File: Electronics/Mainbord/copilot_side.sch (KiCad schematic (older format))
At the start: 30 parts, among them U50 74HC165, U51 74HC165, U52 74HC165, U53 74HC165, U54 4067, U55 74HC4051

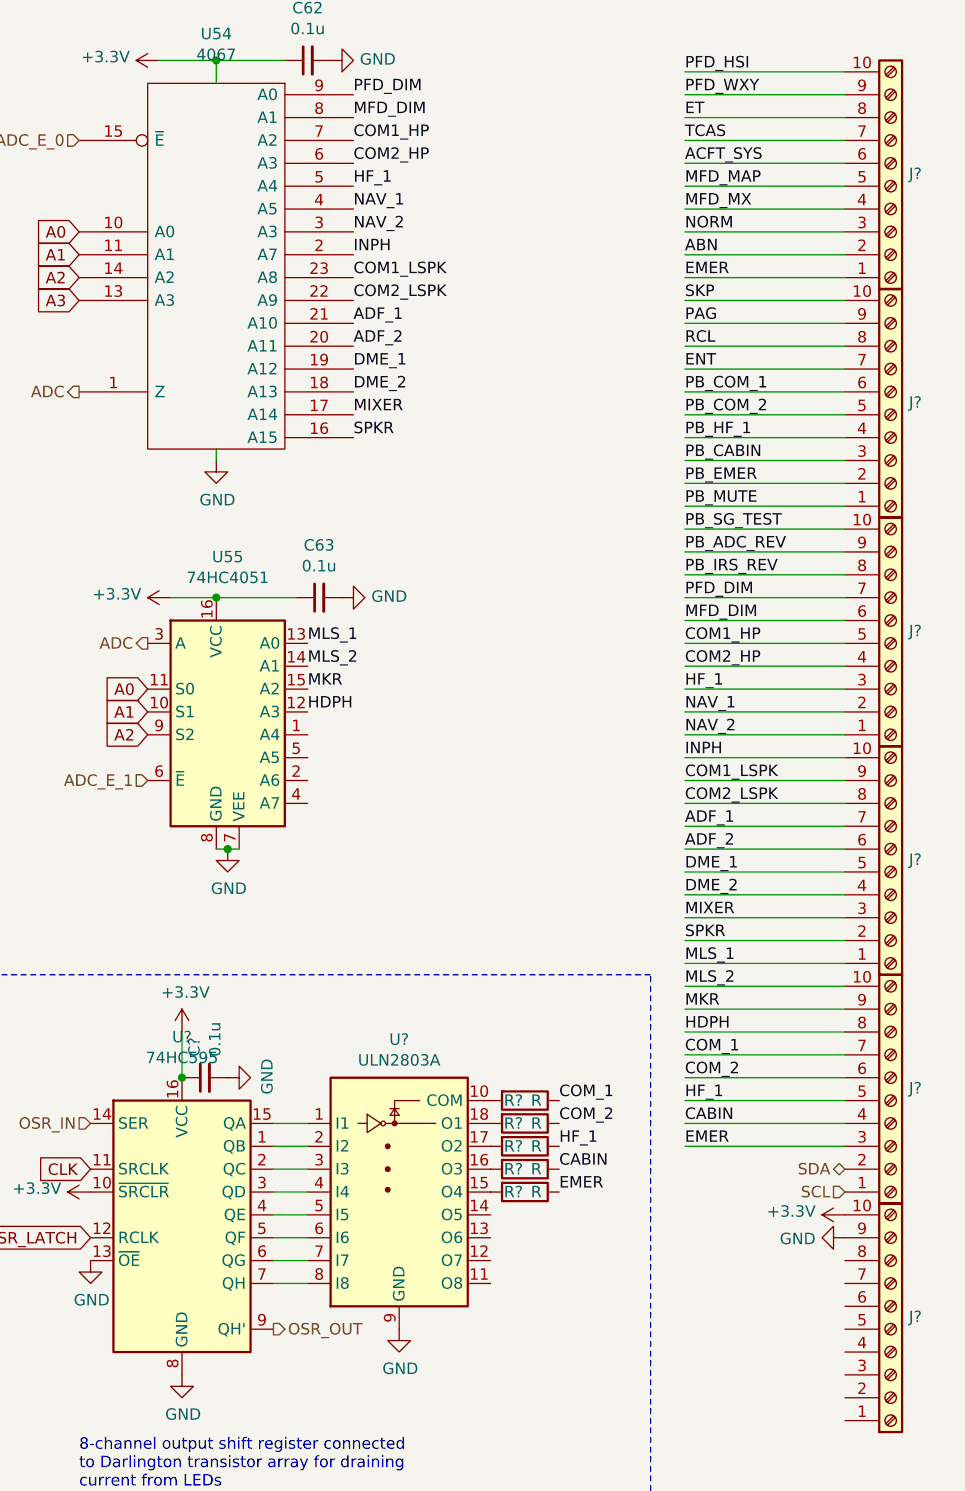
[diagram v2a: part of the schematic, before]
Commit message: Electronics - Adds LCSC part numbers and footprints
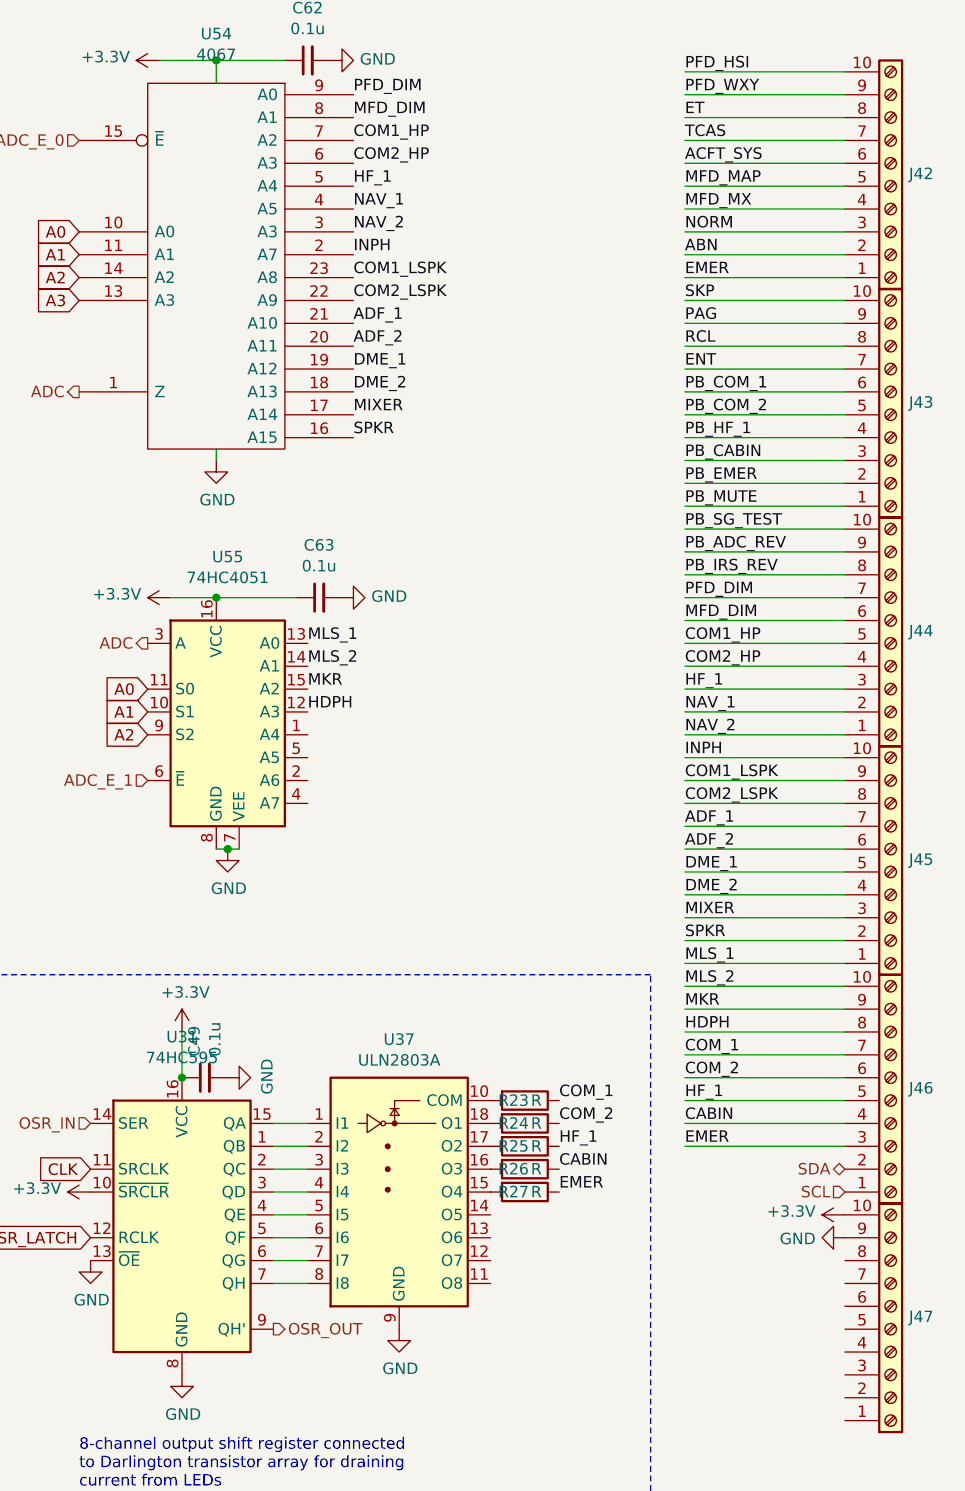
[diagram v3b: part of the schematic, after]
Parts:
- gave numbers to parts that had none: 14
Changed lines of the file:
@@
 AR Path="/5DB6029E/5DF7CBB3" Ref="J?"  Part="1"
 AR Path="/5DC174D4/5DF7CBB3" Ref="J?"  Part="1"
-AR Path="/5DC31399/5DF7CBB3" Ref="J?"  Part="1"
-F 0 "J?" H 8680 1546 50  0000 L CNN
+AR Path="/5DC31399/5DF7CBB3" Ref="J42"  Part="1"
+F 0 "J42" H 8680 1546 50  0000 L CNN
 F 1 "Screw_Terminal_01x10" H 8520 966 50  0001 C CNN
 F 2 "" H 8600 1600 50  0001 C CNN
@@
 AR Path="/5DB6029E/5DF7CBCA" Ref="J?"  Part="1"
 AR Path="/5DC174D4/5DF7CBCA" Ref="J?"  Part="1"
-AR Path="/5DC31399/5DF7CBCA" Ref="J?"  Part="1"
-F 0 "J?" H 8680 2546 50  0000 L CNN
+AR Path="/5DC31399/5DF7CBCA" Ref="J43"  Part="1"
+F 0 "J43" H 8680 2546 50  0000 L CNN
 F 1 "Screw_Terminal_01x10" H 8520 1966 50  0001 C CNN
 F 2 "" H 8600 2600 50  0001 C CNN
@@
 AR Path="/5DB6029E/5DF7CBF0" Ref="J?"  Part="1"
 AR Path="/5DC174D4/5DF7CBF0" Ref="J?"  Part="1"
-AR Path="/5DC31399/5DF7CBF0" Ref="J?"  Part="1"
-F 0 "J?" H 8680 3546 50  0000 L CNN
+AR Path="/5DC31399/5DF7CBF0" Ref="J44"  Part="1"
+F 0 "J44" H 8680 3546 50  0000 L CNN
 F 1 "Screw_Terminal_01x10" H 8520 2966 50  0001 C CNN
 F 2 "" H 8600 3600 50  0001 C CNN
@@
 AR Path="/5DB6029E/5DF7CBFD" Ref="J?"  Part="1"
 AR Path="/5DC174D4/5DF7CBFD" Ref="J?"  Part="1"
-AR Path="/5DC31399/5DF7CBFD" Ref="J?"  Part="1"
-F 0 "J?" H 8680 4546 50  0000 L CNN
+AR Path="/5DC31399/5DF7CBFD" Ref="J45"  Part="1"
+F 0 "J45" H 8680 4546 50  0000 L CNN
 F 1 "Screw_Terminal_01x10" H 8520 3966 50  0001 C CNN
 F 2 "" H 8600 4600 50  0001 C CNN
@@
 AR Path="/5DB6029E/5DF7CC14" Ref="J?"  Part="1"
 AR Path="/5DC174D4/5DF7CC14" Ref="J?"  Part="1"
-AR Path="/5DC31399/5DF7CC14" Ref="J?"  Part="1"
-F 0 "J?" H 8680 5546 50  0000 L CNN
+AR Path="/5DC31399/5DF7CC14" Ref="J46"  Part="1"
+F 0 "J46" H 8680 5546 50  0000 L CNN
 F 1 "Screw_Terminal_01x10" H 8520 4966 50  0001 C CNN
 F 2 "" H 8600 5600 50  0001 C CNN
@@
 AR Path="/5DB6029E/5DF95124" Ref="J?"  Part="1"
 AR Path="/5DC174D4/5DF95124" Ref="J?"  Part="1"
-AR Path="/5DC31399/5DF95124" Ref="J?"  Part="1"
-F 0 "J?" H 8680 6546 50  0000 L CNN
+AR Path="/5DC31399/5DF95124" Ref="J47"  Part="1"
+F 0 "J47" H 8680 6546 50  0000 L CNN
 F 1 "Screw_Terminal_01x10" H 8520 5966 50  0001 C CNN
 F 2 "" H 8600 6600 50  0001 C CNN
@@
 AR Path="/5DB5DCD1/5DFA1204" Ref="#PWR?"  Part="1"
 AR Path="/5DC174D4/5DFA1204" Ref="#PWR?"  Part="1"
-AR Path="/5DC31399/5DFA1204" Ref="#PWR?"  Part="1"
-F 0 "#PWR?" H 8400 5950 50  0001 C CNN
+AR Path="/5DC31399/5DFA1204" Ref="#PWR0279"  Part="1"
+F 0 "#PWR0279" H 8400 5950 50  0001 C CNN
 F 1 "+3.3V" V 8415 6228 50  0000 L CNN
 F 2 "" H 8400 6100 50  0001 C CNN
@@
 AR Path="/5DB5DCD1/5DFA1241" Ref="#PWR?"  Part="1"
 AR Path="/5DC174D4/5DFA1241" Ref="#PWR?"  Part="1"
-AR Path="/5DC31399/5DFA1241" Ref="#PWR?"  Part="1"
-F 0 "#PWR?" H 8400 5950 50  0001 C CNN
+AR Path="/5DC31399/5DFA1241" Ref="#PWR0280"  Part="1"
+F 0 "#PWR0280" H 8400 5950 50  0001 C CNN
 F 1 "GND" V 8405 6072 50  0000 R CNN
 F 2 "" H 8400 6200 50  0001 C CNN
@@
 AR Path="/5DB5DCD1/5E013912" Ref="C?"  Part="1"
 AR Path="/5DC174D4/5E013912" Ref="C?"  Part="1"
-AR Path="/5DC31399/5E013912" Ref="C?"  Part="1"
-F 0 "C?" H 5692 5546 50  0000 L CNN
+AR Path="/5DC31399/5E013912" Ref="C49"  Part="1"
+F 0 "C49" H 5692 5546 50  0000 L CNN
 F 1 "0.1u" H 5692 5455 50  0000 L CNN
 F 2 "" H 5600 5500 50  0001 C CNN
@@
 AR Path="/5DB5DCD1/5E013919" Ref="#PWR?"  Part="1"
 AR Path="/5DC174D4/5E013919" Ref="#PWR?"  Part="1"
-AR Path="/5DC31399/5E013919" Ref="#PWR?"  Part="1"
-F 0 "#PWR?" H 5700 5250 50  0001 C CNN
+AR Path="/5DC31399/5E013919" Ref="#PWR0281"  Part="1"
+F 0 "#PWR0281" H 5700 5250 50  0001 C CNN
 F 1 "GND" H 5705 5327 50  0000 C CNN
 F 2 "" H 5700 5500 50  0001 C CNN
@@
 AR Path="/5DB5DCD1/5E013920" Ref="U?"  Part="1"
 AR Path="/5DC174D4/5E013920" Ref="U?"  Part="1"
-AR Path="/5DC31399/5E013920" Ref="U?"  Part="1"
-F 0 "U?" H 5500 6878 50  0000 C CNN
+AR Path="/5DC31399/5E013920" Ref="U31"  Part="1"
+F 0 "U31" H 5500 6878 50  0000 C CNN
 F 1 "74HC595" H 5500 6787 50  0000 C CNN
 F 2 "" H 5500 6100 50  0001 C CNN
@@
 AR Path="/5DB5DCD1/5E013928" Ref="#PWR?"  Part="1"
 AR Path="/5DC174D4/5E013928" Ref="#PWR?"  Part="1"
-AR Path="/5DC31399/5E013928" Ref="#PWR?"  Part="1"
-F 0 "#PWR?" H 5500 6550 50  0001 C CNN
+AR Path="/5DC31399/5E013928" Ref="#PWR0282"  Part="1"
+F 0 "#PWR0282" H 5500 6550 50  0001 C CNN
 F 1 "GND" H 5505 6627 50  0000 C CNN
 F 2 "" H 5500 6800 50  0001 C CNN
@@
 AR Path="/5DB5DCD1/5E01392F" Ref="#PWR?"  Part="1"
 AR Path="/5DC174D4/5E01392F" Ref="#PWR?"  Part="1"
-AR Path="/5DC31399/5E01392F" Ref="#PWR?"  Part="1"
-F 0 "#PWR?" H 5100 6050 50  0001 C CNN
+AR Path="/5DC31399/5E01392F" Ref="#PWR0283"  Part="1"
+F 0 "#PWR0283" H 5100 6050 50  0001 C CNN
 F 1 "GND" H 5105 6127 50  0000 C CNN
 F 2 "" H 5100 6300 50  0001 C CNN
@@
 AR Path="/5DB5DCD1/5E013936" Ref="#PWR?"  Part="1"
 AR Path="/5DC174D4/5E013936" Ref="#PWR?"  Part="1"
-AR Path="/5DC31399/5E013936" Ref="#PWR?"  Part="1"
-F 0 "#PWR?" H 5500 5150 50  0001 C CNN
+AR Path="/5DC31399/5E013936" Ref="#PWR0284"  Part="1"
+F 0 "#PWR0284" H 5500 5150 50  0001 C CNN
 F 1 "+3.3V" H 5515 5473 50  0000 C CNN
 F 2 "" H 5500 5300 50  0001 C CNN
@@
 AR Path="/5DB5DCD1/5E01393C" Ref="#PWR?"  Part="1"
 AR Path="/5DC174D4/5E01393C" Ref="#PWR?"  Part="1"
-AR Path="/5DC31399/5E01393C" Ref="#PWR?"  Part="1"
-F 0 "#PWR?" H 5100 5850 50  0001 C CNN
+AR Path="/5DC31399/5E01393C" Ref="#PWR0306"  Part="1"
+F 0 "#PWR0306" H 5100 5850 50  0001 C CNN
 F 1 "+3.3V" V 5115 6128 50  0000 L CNN
 F 2 "" H 5100 6000 50  0001 C CNN
@@
 AR Path="/5DBF6FEB/5E01394A" Ref="U?"  Part="1"
 AR Path="/5DC33C09/5E01394A" Ref="U?"  Part="1"
-AR Path="/5DC31399/5E01394A" Ref="U?"  Part="1"
+AR Path="/5DC31399/5E01394A" Ref="U37"  Part="1"
 AR Path="/5DC174D4/5E01394A" Ref="U?"  Part="1"
-F 0 "U?" H 6450 6467 50  0000 C CNN
+F 0 "U37" H 6450 6467 50  0000 C CNN
 F 1 "ULN2803A" H 6450 6376 50  0000 C CNN
 F 2 "" H 6500 5250 50  0001 L CNN
@@
 AR Path="/5DB5DCD1/5E013951" Ref="#PWR?"  Part="1"
 AR Path="/5DC174D4/5E013951" Ref="#PWR?"  Part="1"
-AR Path="/5DC31399/5E013951" Ref="#PWR?"  Part="1"
-F 0 "#PWR?" H 6450 6350 50  0001 C CNN
+AR Path="/5DC31399/5E013951" Ref="#PWR0307"  Part="1"
+F 0 "#PWR0307" H 6450 6350 50  0001 C CNN
 F 1 "GND" H 6455 6427 50  0000 C CNN
 F 2 "" H 6450 6600 50  0001 C CNN
@@
 P 7000 5600
 AR Path="/5DC33C09/5E013957" Ref="R?"  Part="1"
-AR Path="/5DC31399/5E013957" Ref="R?"  Part="1"
+AR Path="/5DC31399/5E013957" Ref="R23"  Part="1"
 AR Path="/5DC174D4/5E013957" Ref="R?"  Part="1"
-F 0 "R?" V 7000 5550 50  0000 C CNN
+F 0 "R23" V 7000 5550 50  0000 C CNN
 F 1 "R" V 7000 5650 50  0000 C CNN
 F 2 "" V 6930 5600 50  0001 C CNN
@@
 P 7000 5700
 AR Path="/5DC33C09/5E01395E" Ref="R?"  Part="1"
-AR Path="/5DC31399/5E01395E" Ref="R?"  Part="1"
+AR Path="/5DC31399/5E01395E" Ref="R24"  Part="1"
 AR Path="/5DC174D4/5E01395E" Ref="R?"  Part="1"
-F 0 "R?" V 7000 5650 50  0000 C CNN
+F 0 "R24" V 7000 5650 50  0000 C CNN
 F 1 "R" V 7000 5750 50  0000 C CNN
 F 2 "" V 6930 5700 50  0001 C CNN
@@
 P 7000 5800
 AR Path="/5DC33C09/5E013965" Ref="R?"  Part="1"
-AR Path="/5DC31399/5E013965" Ref="R?"  Part="1"
+AR Path="/5DC31399/5E013965" Ref="R25"  Part="1"
 AR Path="/5DC174D4/5E013965" Ref="R?"  Part="1"
-F 0 "R?" V 7000 5750 50  0000 C CNN
+F 0 "R25" V 7000 5750 50  0000 C CNN
 F 1 "R" V 7000 5850 50  0000 C CNN
 F 2 "" V 6930 5800 50  0001 C CNN
@@
 P 7000 5900
 AR Path="/5DC33C09/5E01396C" Ref="R?"  Part="1"
-AR Path="/5DC31399/5E01396C" Ref="R?"  Part="1"
+AR Path="/5DC31399/5E01396C" Ref="R26"  Part="1"
 AR Path="/5DC174D4/5E01396C" Ref="R?"  Part="1"
-F 0 "R?" V 7000 5850 50  0000 C CNN
+F 0 "R26" V 7000 5850 50  0000 C CNN
 F 1 "R" V 7000 5950 50  0000 C CNN
 F 2 "" V 6930 5900 50  0001 C CNN
@@
 P 7000 6000
 AR Path="/5DC33C09/5E013973" Ref="R?"  Part="1"
-AR Path="/5DC31399/5E013973" Ref="R?"  Part="1"
+AR Path="/5DC31399/5E013973" Ref="R27"  Part="1"
 AR Path="/5DC174D4/5E013973" Ref="R?"  Part="1"
-F 0 "R?" V 7000 5950 50  0000 C CNN
+F 0 "R27" V 7000 5950 50  0000 C CNN
 F 1 "R" V 7000 6050 50  0000 C CNN
 F 2 "" V 6930 6000 50  0001 C CNN
